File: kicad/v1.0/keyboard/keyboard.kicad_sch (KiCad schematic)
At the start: 16 parts, among them J1 NumPad, J2 PMOD, U1 74LS165, U2 74LS165, U3 74LS165, U4 74LS165, U5 74LS165, U6 74LS165, U7 74LS165

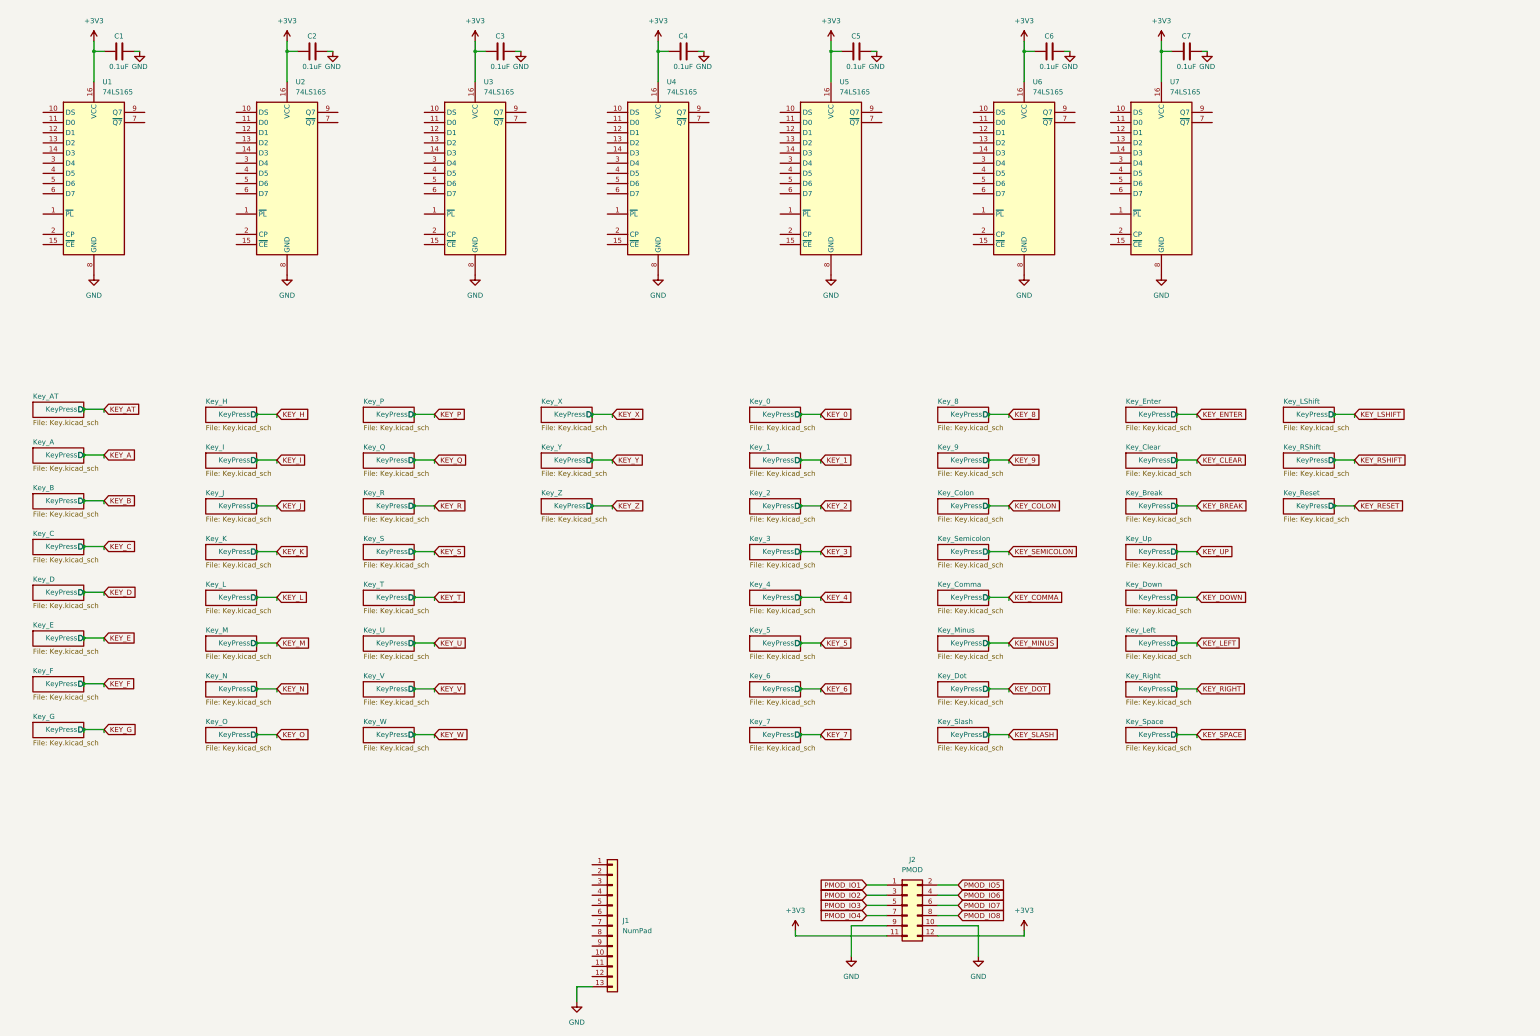
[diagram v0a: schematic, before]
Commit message: Positioning
- Added Library
- Created Footprint for 2-pin push-button
- Added additional keys for ENTER and SPACE to cover whole length
- Added keys for numpad (1:1 link to other number keys)
- Positioned main keys, numpad keys
- Created cutout for reset switch
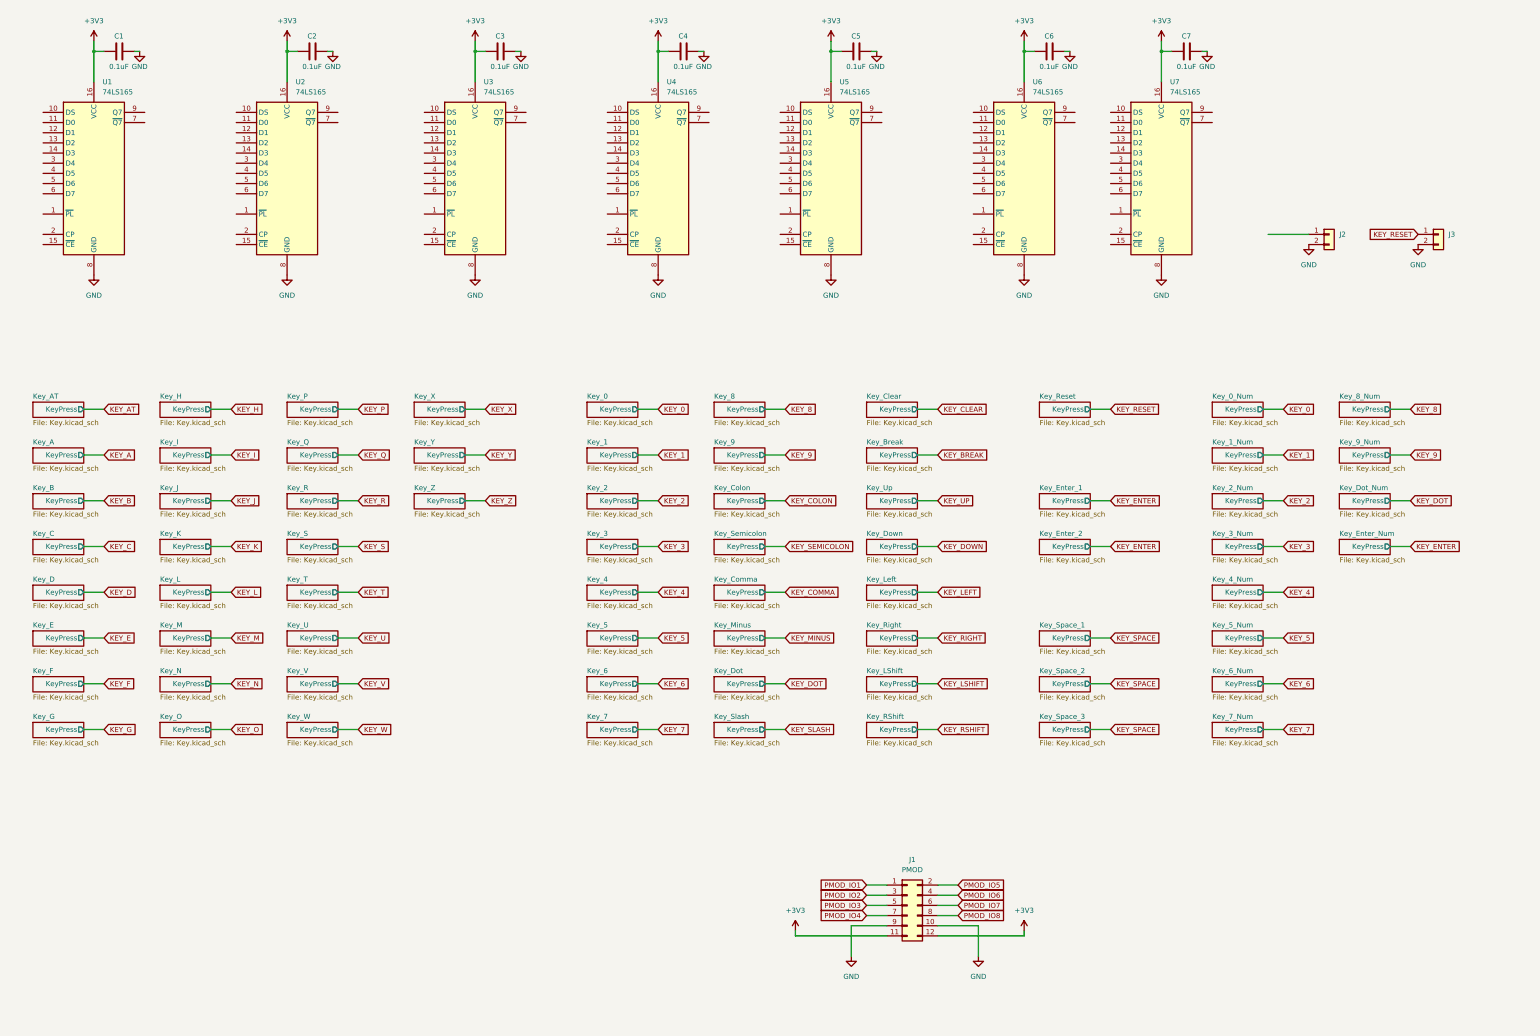
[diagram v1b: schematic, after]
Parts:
- removed J1: NumPad, Connector_PinHeader_2.54mm:PinHeader_1x13_P2.54mm_Vertical, symbol Connector_Generic:Conn_01x13
- added J2, J3: Conn_01x02, Connector_PinHeader_2.54mm:PinHeader_1x02_P2.54mm_Vertical, symbol Connector_Generic:Conn_01x02
- renumbered J2 to J1
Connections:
- net GND: now also J2.2 (Pin_2), J3.2 (Pin_2)
- net KEY_RESET: now also J3.1 (Pin_1)
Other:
- sheet Key_Enter renamed Key_Enter_1
- sheet Key_Space renamed Key_Space_1
- added sheet Key_0_Num (Key.kicad_sch)
- added sheet Key_1_Num (Key.kicad_sch)
- added sheet Key_2_Num (Key.kicad_sch)
- added sheet Key_3_Num (Key.kicad_sch)
- added sheet Key_4_Num (Key.kicad_sch)
- added sheet Key_5_Num (Key.kicad_sch)
- added sheet Key_6_Num (Key.kicad_sch)
- added sheet Key_7_Num (Key.kicad_sch)
- added sheet Key_8_Num (Key.kicad_sch)
- added sheet Key_9_Num (Key.kicad_sch)
- added sheet Key_Dot_Num (Key.kicad_sch)
- added sheet Key_Enter_2 (Key.kicad_sch)
- added sheet Key_Enter_Num (Key.kicad_sch)
- added sheet Key_Space_2 (Key.kicad_sch)
- added sheet Key_Space_3 (Key.kicad_sch)

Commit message: Redesign of Keyboard
This is a new design of the keyboard that is based on the TRS-80 Model 1 keyboard interface design.
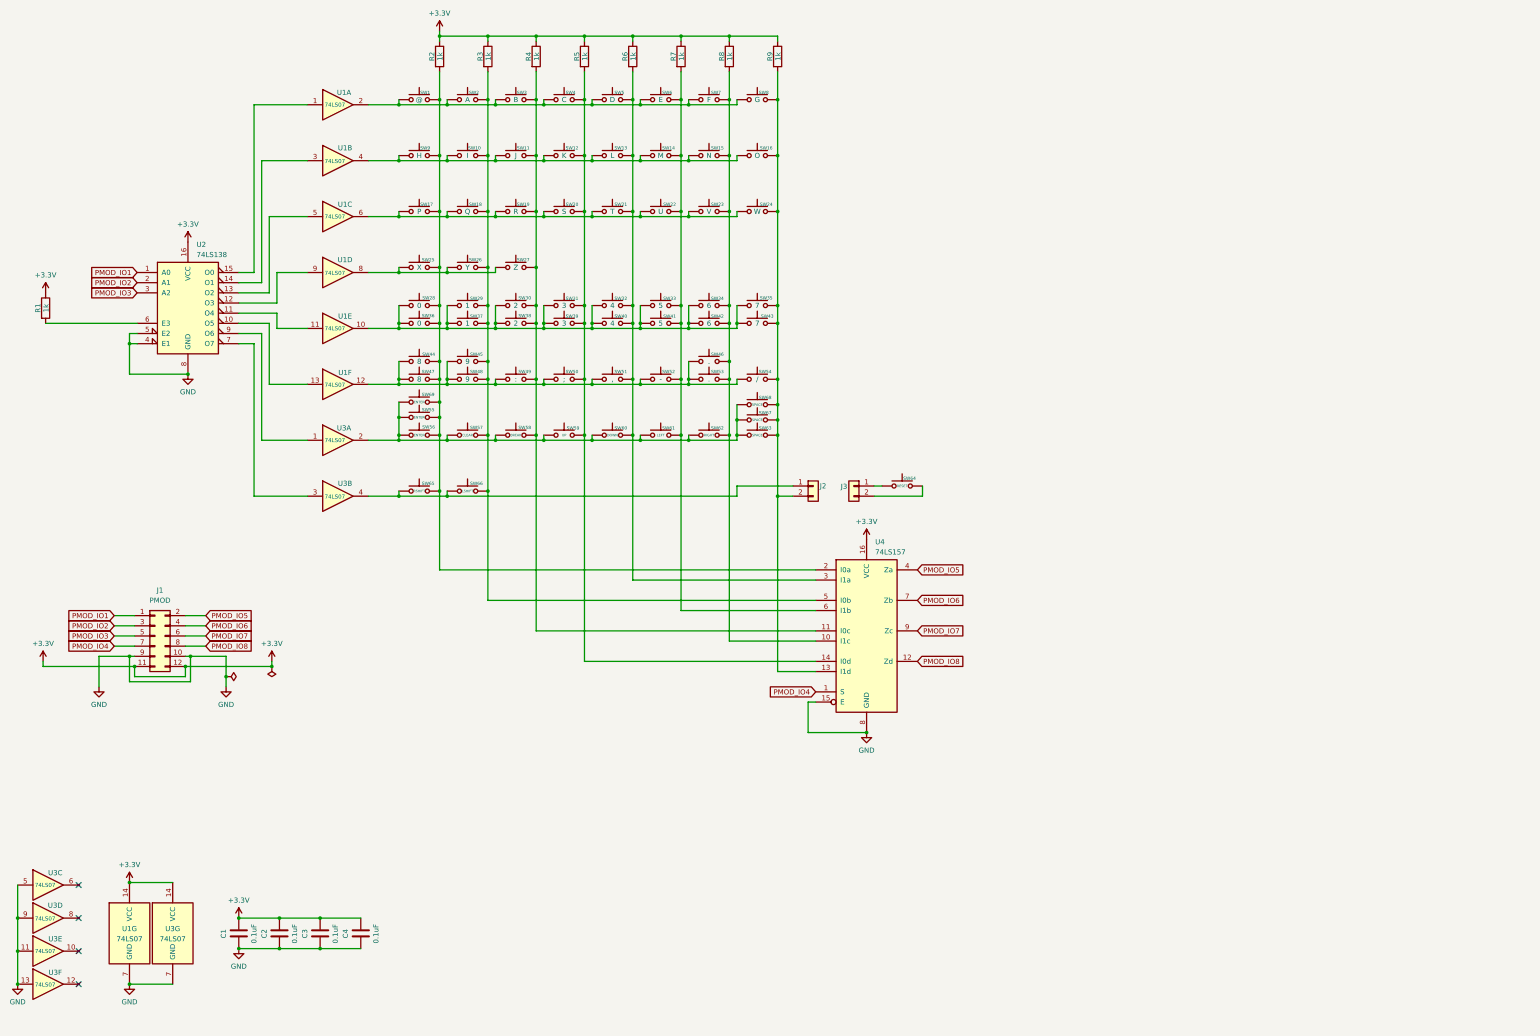
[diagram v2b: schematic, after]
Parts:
- removed C5, C6, C7: 0.1uF, Capacitor_SMD:C_0805_2012Metric_Pad1.18x1.45mm_HandSolder, symbol Device:C
- removed U1, U2, U3, U4, U5, U6, U7: 74LS165, Package_SO:SOIC-16_3.9x9.9mm_P1.27mm, symbol 74xx:74LS165
- added R1, R2, R3, R4, R5, R6, R7, R8, R9: 1k, Resistor_SMD:R_0805_2012Metric_Pad1.20x1.40mm_HandSolder, symbol Device:R
- added SW1: @, Library:SW_SPST_Push, symbol Switch:SW_Push
- added SW10: I, Library:SW_SPST_Push, symbol Switch:SW_Push
- added SW11: J, Library:SW_SPST_Push, symbol Switch:SW_Push
- added SW12: K, Library:SW_SPST_Push, symbol Switch:SW_Push
- added SW13: L, Library:SW_SPST_Push, symbol Switch:SW_Push
- added SW14: M, Library:SW_SPST_Push, symbol Switch:SW_Push
- added SW15: N, Library:SW_SPST_Push, symbol Switch:SW_Push
- added SW16: O, Library:SW_SPST_Push, symbol Switch:SW_Push
- added SW17: P, Library:SW_SPST_Push, symbol Switch:SW_Push
- added SW18: Q, Library:SW_SPST_Push, symbol Switch:SW_Push
- added SW19: R, Library:SW_SPST_Push, symbol Switch:SW_Push
- added SW2: A, Library:SW_SPST_Push, symbol Switch:SW_Push
- added SW20: S, Library:SW_SPST_Push, symbol Switch:SW_Push
- added SW21: T, Library:SW_SPST_Push, symbol Switch:SW_Push
- added SW22: U, Library:SW_SPST_Push, symbol Switch:SW_Push
- added SW23: V, Library:SW_SPST_Push, symbol Switch:SW_Push
- added SW24: W, Library:SW_SPST_Push, symbol Switch:SW_Push
- added SW25: X, Library:SW_SPST_Push, symbol Switch:SW_Push
- added SW26: Y, Library:SW_SPST_Push, symbol Switch:SW_Push
- added SW27: Z, Library:SW_SPST_Push, symbol Switch:SW_Push
- added SW28, SW36: 0, Library:SW_SPST_Push, symbol Switch:SW_Push
- added SW29, SW37: 1, Library:SW_SPST_Push, symbol Switch:SW_Push
- added SW3: B, Library:SW_SPST_Push, symbol Switch:SW_Push
- added SW30, SW38: 2, Library:SW_SPST_Push, symbol Switch:SW_Push
- added SW31, SW39: 3, Library:SW_SPST_Push, symbol Switch:SW_Push
- added SW32, SW40: 4, Library:SW_SPST_Push, symbol Switch:SW_Push
- added SW33, SW41: 5, Library:SW_SPST_Push, symbol Switch:SW_Push
- added SW34, SW42: 6, Library:SW_SPST_Push, symbol Switch:SW_Push
- added SW35, SW43: 7, Library:SW_SPST_Push, symbol Switch:SW_Push
- added SW4: C, Library:SW_SPST_Push, symbol Switch:SW_Push
- added SW44, SW47: 8, Library:SW_SPST_Push, symbol Switch:SW_Push
- added SW45, SW48: 9, Library:SW_SPST_Push, symbol Switch:SW_Push
- added SW46, SW53: ., Library:SW_SPST_Push, symbol Switch:SW_Push
- added SW49: :, Library:SW_SPST_Push, symbol Switch:SW_Push
- added SW5: D, Library:SW_SPST_Push, symbol Switch:SW_Push
- added SW50: ;, Library:SW_SPST_Push, symbol Switch:SW_Push
- added SW51: ,, Library:SW_SPST_Push, symbol Switch:SW_Push
- added SW52: -, Library:SW_SPST_Push, symbol Switch:SW_Push
- added SW54: /, Library:SW_SPST_Push, symbol Switch:SW_Push
- added SW55, SW56, SW69: ENTER, Library:SW_SPST_Push, symbol Switch:SW_Push
- added SW57: CLEAR, Library:SW_SPST_Push, symbol Switch:SW_Push
- added SW58: BREAK, Library:SW_SPST_Push, symbol Switch:SW_Push
- added SW59: UP, Library:SW_SPST_Push, symbol Switch:SW_Push
- added SW6: E, Library:SW_SPST_Push, symbol Switch:SW_Push
- added SW60: DOWN, Library:SW_SPST_Push, symbol Switch:SW_Push
- added SW61: LEFT, Library:SW_SPST_Push, symbol Switch:SW_Push
- added SW62: RIGHT, Library:SW_SPST_Push, symbol Switch:SW_Push
- added SW63, SW67, SW68: SPACE, Library:SW_SPST_Push, symbol Switch:SW_Push
- added SW64: RESET, Library:SW_SPST_Push, symbol Switch:SW_Push
- added SW65: RSHIFT, Library:SW_SPST_Push, symbol Switch:SW_Push
- added SW66: LSHIFT, Library:SW_SPST_Push, symbol Switch:SW_Push
- added SW7: F, Library:SW_SPST_Push, symbol Switch:SW_Push
- added SW8: G, Library:SW_SPST_Push, symbol Switch:SW_Push
- added SW9: H, Library:SW_SPST_Push, symbol Switch:SW_Push
- added U1, U3: 74LS07, Package_SO:SOIC-14_3.9x8.7mm_P1.27mm, symbol 74xx:74LS07
- added U2: 74LS138, Package_SO:SOIC-16_3.9x9.9mm_P1.27mm, symbol 74xx:74LS138
- added U4: 74LS157, Package_SO:SOIC-16_3.9x9.9mm_P1.27mm, symbol 74xx:74LS157
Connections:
- net GND: now also C1.2, C2.2, C3.2, C4.2, U1.7 (GND), U2.4 (E1), U2.5 (E2), U2.8 (GND), U3.11, U3.13, U3.5, U3.7 (GND), U3.9, U4.15 (E), U4.8 (GND); no longer C1.1, C2.1, C3.1, C4.1, J2.2 (Pin_2), J3.2 (Pin_2)
- net PMOD_IO1: now also U2.1 (A0)
- net PMOD_IO2: now also U2.2 (A1)
- net PMOD_IO3: now also U2.3 (A2)
- net PMOD_IO4: now also U4.1 (S)
- net PMOD_IO5: now also U4.4 (Za)
- net PMOD_IO6: now also U4.7 (Zb)
- net PMOD_IO7: now also U4.9 (Zc)
- net PMOD_IO8: now also U4.12 (Zd)
- net at J2.1 (Pin_1): now also SW65.1, SW66.2, U3.4
- removed net +3V3: C1.2, C2.2, C3.2, C4.2, J1.11 (Pin_11), J1.12 (Pin_12)
- net KEY_RESET: no longer names the net of J3.1 (Pin_1)
- net KEY_RESET: now also SW64.2
- new net: SW44.2, SW45.2, SW46.1, SW47.1, SW48.2, SW49.1, SW50.1, SW51.1, SW52.2, SW53.1, SW54.2, U1.12
- new net: R6.2, SW13.1, SW21.2, SW32.1, SW40.1, SW5.2, SW51.2, SW60.1, U4.3 (I1a)
- new net: SW1.2, SW2.1, SW3.2, SW4.2, SW5.1, SW6.1, SW7.1, SW8.2, U1.2
- new net: R7.2, SW14.2, SW22.2, SW33.1, SW41.1, SW52.1, SW6.2, SW61.2, U4.6 (I1b)
- new net: U2.9 (O6), U3.1
- new net: SW55.1, SW56.2, SW57.1, SW58.1, SW59.1, SW60.2, SW61.1, SW62.2, SW63.2, SW67.2, SW68.2, SW69.1, U3.2
- new net: SW10.2, SW11.2, SW12.1, SW13.2, SW14.1, SW15.1, SW16.1, SW9.2, U1.4
- new net: R2.2, SW1.1, SW17.1, SW25.2, SW28.1, SW36.2, SW44.1, SW47.2, SW55.2, SW56.1, SW65.2, SW69.2, SW9.1, U4.2 (I0a)
- new net: SW28.2, SW29.2, SW30.1, SW31.2, SW32.2, SW33.2, SW34.2, SW35.1, SW36.1, SW37.2, SW38.1, SW39.2, SW40.2, SW41.2, SW42.2, SW43.2, U1.10
- new net: J2.2 (Pin_2), R9.2, SW16.2, SW24.1, SW35.2, SW43.1, SW54.1, SW63.1, SW67.1, SW68.1, SW8.1, U4.13 (I1d)
- new net: R8.2, SW15.2, SW23.2, SW34.1, SW42.1, SW46.2, SW53.2, SW62.1, SW7.2, U4.10 (I1c)
- new net: R4.2, SW11.1, SW19.2, SW27.1, SW3.1, SW30.2, SW38.2, SW49.2, SW58.2, U4.11 (I0c)
- new net: U1.11, U2.11 (O4)
- new net: R5.2, SW12.2, SW20.2, SW31.1, SW39.1, SW4.1, SW50.2, SW59.2, U4.14 (I0d)
- new net: R3.2, SW10.1, SW18.1, SW2.2, SW26.1, SW29.1, SW37.1, SW45.1, SW48.1, SW57.2, SW66.1, U4.5 (I0b)
- new net: SW17.2, SW18.2, SW19.1, SW20.1, SW21.1, SW22.1, SW23.1, SW24.2, U1.6
- new net: SW25.1, SW26.2, SW27.2, U1.8
- new net: U1.9, U2.12 (O3)
- new net: J3.2 (Pin_2), SW64.1
- new net: U2.7 (O7), U3.3
- new net: U1.3, U2.14 (O1)
- new net: R1.2, U2.6 (E3)
- new net: U1.5, U2.13 (O2)
- new net: U1.13, U2.10 (O5)
- new net: U1.1, U2.15 (O0)
- new net +3.3V: C1.1, C2.1, C3.1, C4.1, J1.11 (Pin_11), J1.12 (Pin_12), R1.1, R2.1, R3.1, R4.1, R5.1, R6.1, R7.1, R8.1, R9.1, U1.14 (VCC), U2.16 (VCC), U3.14 (VCC), U4.16 (VCC)
- no-connect marks 0 -> 4
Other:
- removed sheet Key_0
- removed sheet Key_0_Num
- removed sheet Key_1
- removed sheet Key_1_Num
- removed sheet Key_2
- removed sheet Key_2_Num
- removed sheet Key_3
- removed sheet Key_3_Num
- removed sheet Key_4
- removed sheet Key_4_Num
- removed sheet Key_5
- removed sheet Key_5_Num
- removed sheet Key_6
- removed sheet Key_6_Num
- removed sheet Key_7
- removed sheet Key_7_Num
- removed sheet Key_8
- removed sheet Key_8_Num
- removed sheet Key_9
- removed sheet Key_9_Num
- removed sheet Key_A
- removed sheet Key_AT
- removed sheet Key_B
- removed sheet Key_Break
- removed sheet Key_C
- removed sheet Key_Clear
- removed sheet Key_Colon
- removed sheet Key_Comma
- removed sheet Key_D
- removed sheet Key_Dot
- removed sheet Key_Dot_Num
- removed sheet Key_Down
- removed sheet Key_E
- removed sheet Key_Enter_1
- removed sheet Key_Enter_2
- removed sheet Key_Enter_Num
- removed sheet Key_F
- removed sheet Key_G
- removed sheet Key_H
- removed sheet Key_I
- removed sheet Key_J
- removed sheet Key_K
- removed sheet Key_L
- removed sheet Key_LShift
- removed sheet Key_Left
- removed sheet Key_M
- removed sheet Key_Minus
- removed sheet Key_N
- removed sheet Key_O
- removed sheet Key_P
- removed sheet Key_Q
- removed sheet Key_R
- removed sheet Key_RShift
- removed sheet Key_Reset
- removed sheet Key_Right
- removed sheet Key_S
- removed sheet Key_Semicolon
- removed sheet Key_Slash
- removed sheet Key_Space_1
- removed sheet Key_Space_2
- removed sheet Key_Space_3
- removed sheet Key_T
- removed sheet Key_U
- removed sheet Key_Up
- removed sheet Key_V
- removed sheet Key_W
- removed sheet Key_X
- removed sheet Key_Y
- removed sheet Key_Z
- moved on the sheet: J1, J2, J3
